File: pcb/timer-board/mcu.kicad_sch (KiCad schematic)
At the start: 7 parts, among them U1 STM32F411RET6

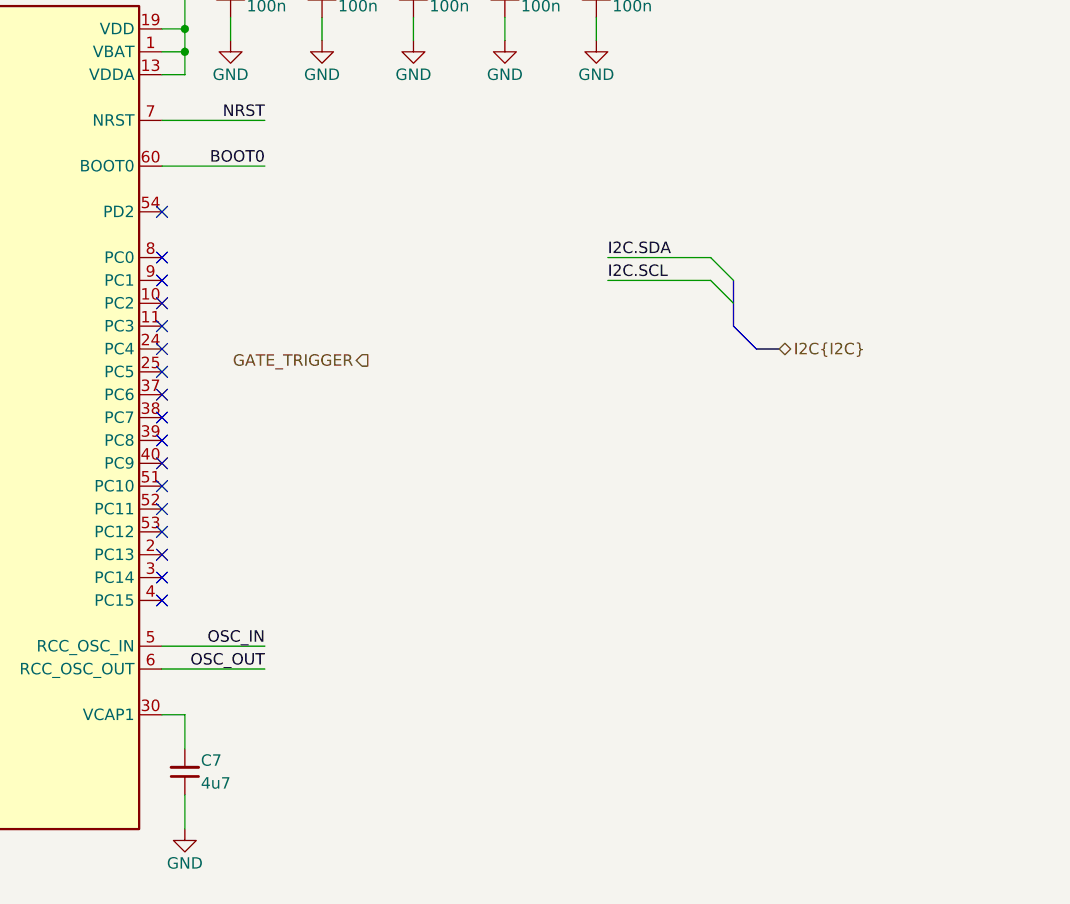
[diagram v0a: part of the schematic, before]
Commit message: Connect OLED display, position main components
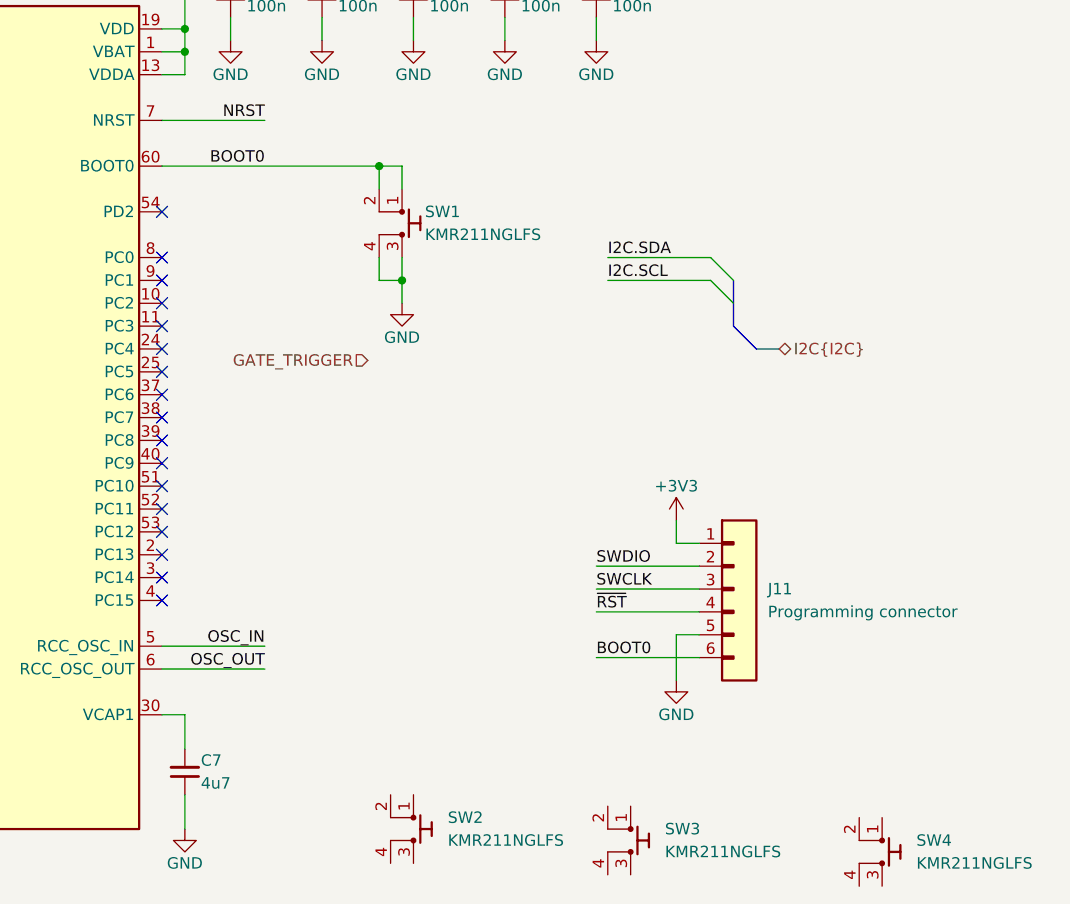
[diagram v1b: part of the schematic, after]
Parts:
- added J11: Programming connector, DW-footprints:Custom-programming-connector-1x6_P1.27mm, symbol DW-connectors:Custom-programming-connector-1x6_P1.27mm
- added SW1, SW2, SW3, SW4: SW_KMR211NGLFS, DW-footprints:SW_KMR211NGLFS, symbol DW-mechanical:SW_KMR211NGLFS
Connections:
- net +3V3: now also J11.1
- net BOOT0: now also J11.6, SW1.1, SW1.2
- net GND: now also J11.5, SW1.3, SW1.4
- net SWCLK: now also J11.3
- net SWDIO: now also J11.2
- new net ~{RST}: J11.4

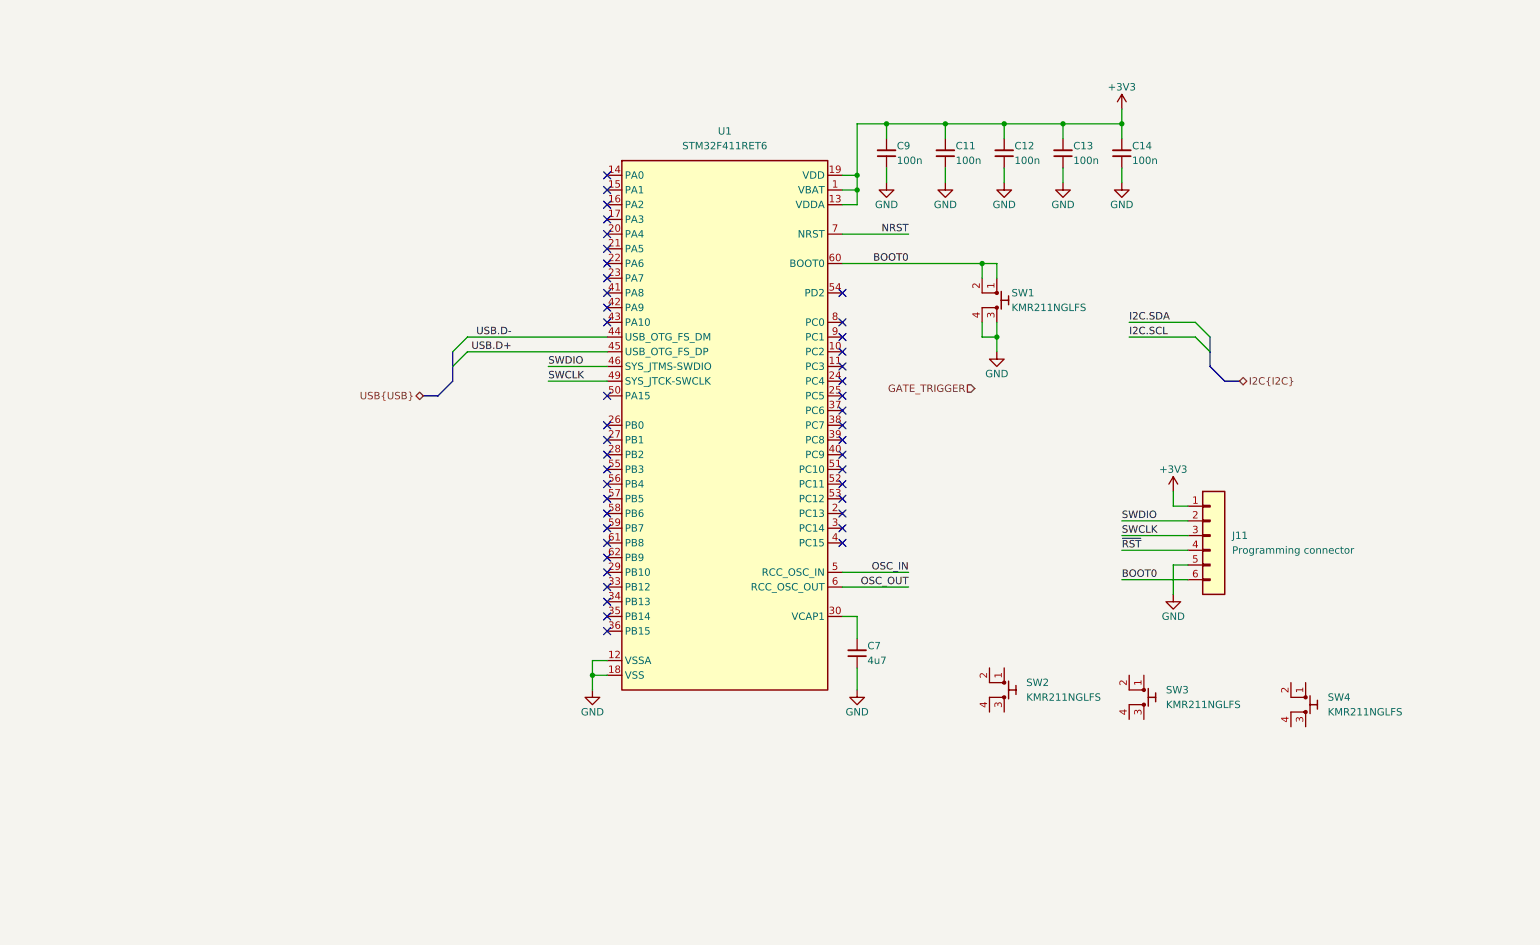
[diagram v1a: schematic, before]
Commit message: Layout power planes and different signals
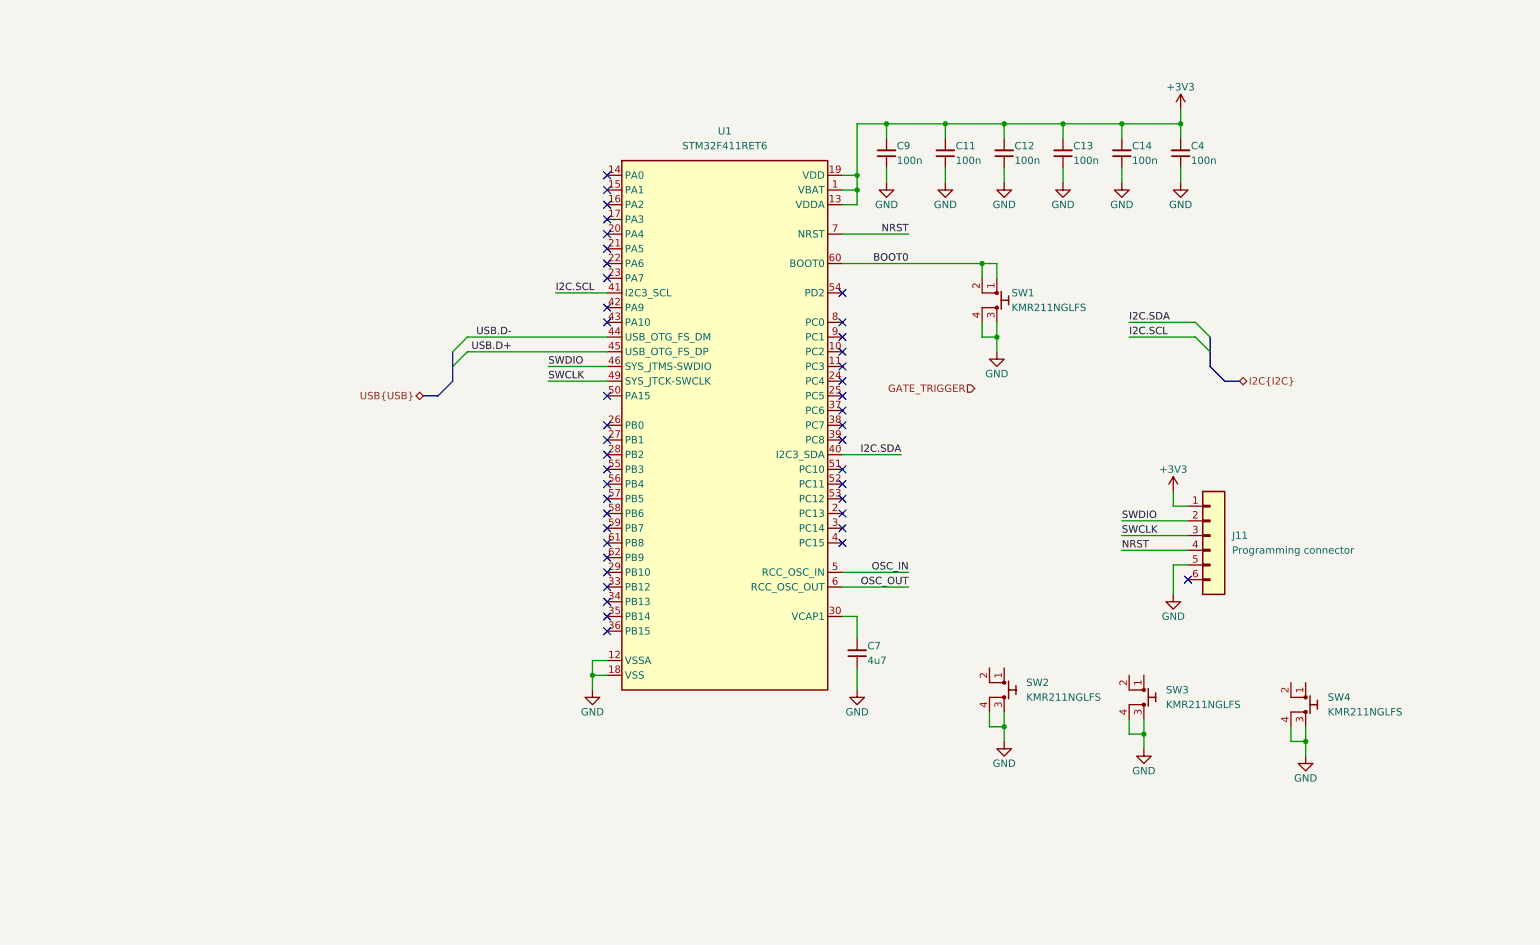
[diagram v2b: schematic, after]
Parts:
- added C4: C-100n-0402, DW-footprints:C_0402_1005Metric, symbol DW-capacitors:C-100n-0402
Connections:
- net ~{RST} is gone; now on net NRST: J11.4
- net +3V3: now also C4.2
- net BOOT0: no longer J11.6
- net GND: now also SW2.3, SW2.4, SW3.3, SW3.4, SW4.3, SW4.4, C4.1
- net I2C.SCL: now also U1.41 (PA8)
- net I2C.SDA: now also U1.40 (PC9)
- no-connect marks 44 -> 43

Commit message: Finish uncompleted schematic sections, layout most of the PCB
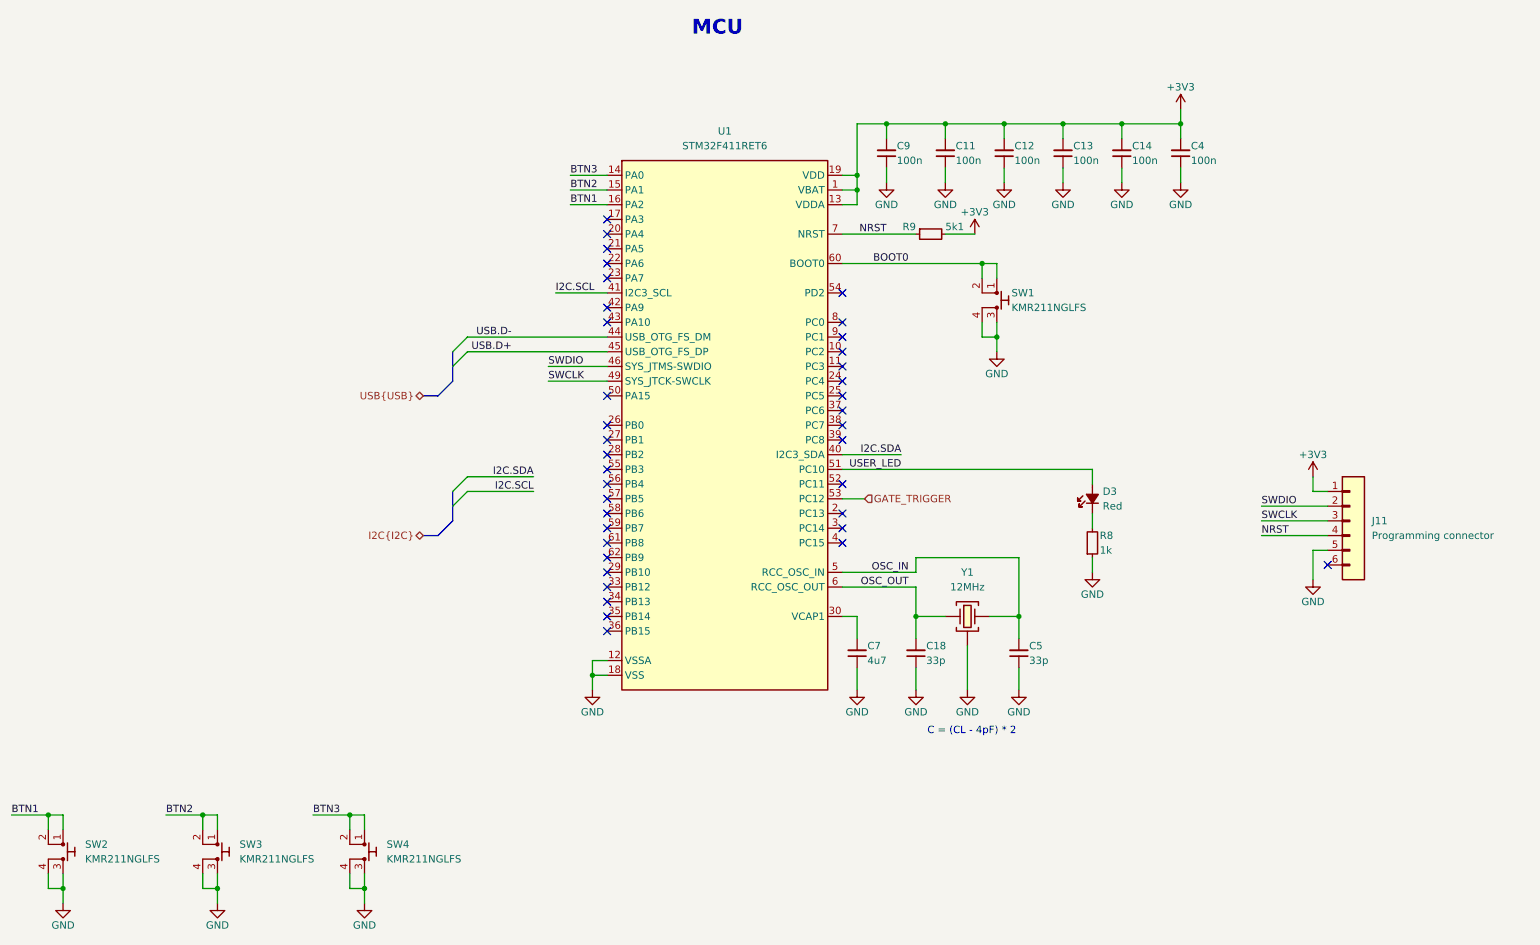
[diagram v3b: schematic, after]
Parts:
- added C18, C5: C-33p-0402, DW-footprints:C_0402_1005Metric, symbol DW-capacitors:C-33p-0402
- added D3: LED-R-0603_KT-0603R, DW-footprints:LED_0603_1608Metric_R, symbol DW-diodes:LED-R-0603_KT-0603R
- added R8: R-1k-0402, DW-footprints:R_0402_1005Metric, symbol DW-resistors:R-1k-0402
- added R9: R-5k1-0402, DW-footprints:R_0402_1005Metric, symbol DW-resistors:R-5k1-0402
- added Y1: X322512MSB4SI, DW-footprints:Crystal_SMD_3225-4Pin_3.2x2.5mm, symbol DW-crystals:Crystal_12MHz_X322512MSB4SI
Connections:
- net +3V3: now also R9.2
- net GATE_TRIGGER: now also U1.53 (PC12)
- net GND: now also C18.1, C5.1, R8.1, Y1.2 (SH), Y1.4 (SH)
- net NRST: now also R9.1
- net OSC_IN: now also C5.2, Y1.3
- net OSC_OUT: now also C18.2, Y1.1
- net BTN3: now reaches SW4.1
- net BTN3: now also SW4.2, U1.14 (PA0)
- net BTN2: now reaches SW3.1
- net BTN2: now also SW3.2, U1.15 (PA1)
- net BTN1: now reaches U1.16 (PA2)
- net BTN1: now also SW2.1, SW2.2
- net USER_LED: now reaches U1.51 (PC10)
- net USER_LED: now also D3.2 (A)
- new net: D3.1 (C), R8.2
- no-connect marks 43 -> 38
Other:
- note added: "C = (CL - 4pF) * 2"
- note added: "MCU"
- moved on the sheet: J11, SW2, SW3, SW4

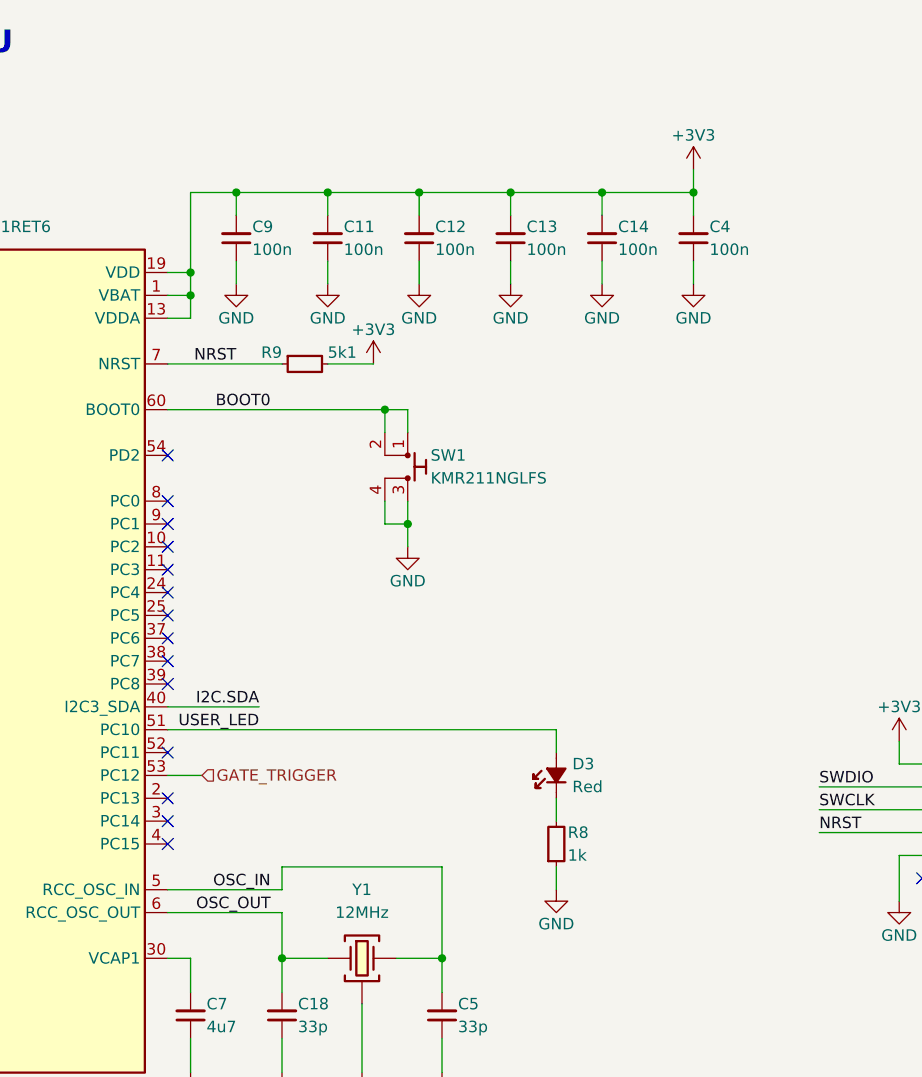
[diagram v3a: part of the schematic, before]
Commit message: Add 3.5mm jack, fix BOOT0 connection
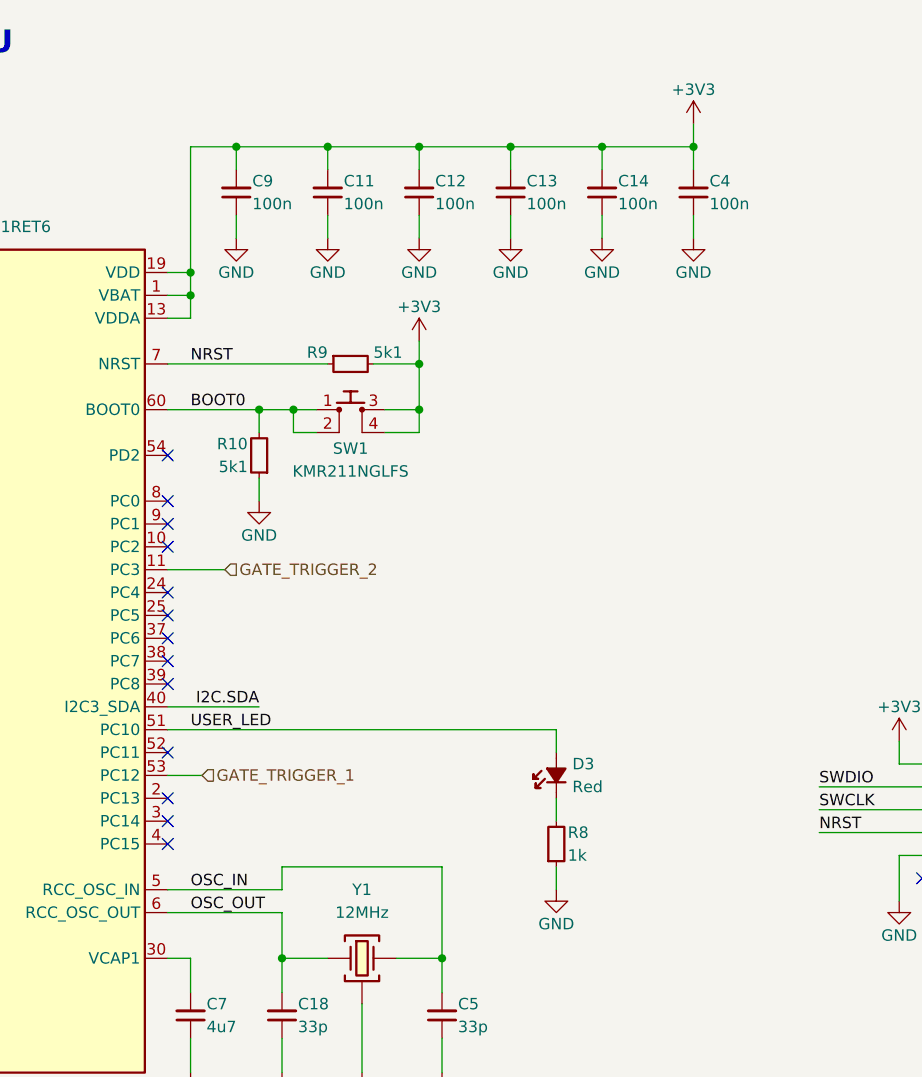
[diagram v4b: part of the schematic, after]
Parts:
- added R10: R-5k1-0402, DW-footprints:R_0402_1005Metric, symbol DW-resistors:R-5k1-0402
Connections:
- net +3V3: now also SW1.3, SW1.4
- net BOOT0: now also R10.2
- net GND: now also R10.1; no longer SW1.3, SW1.4
- net GATE_TRIGGER_2: now reaches U1.11 (PC3)
- net GATE_TRIGGER renamed GATE_TRIGGER_1
- no-connect marks 38 -> 37
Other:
- moved on the sheet: C11, C12, C13, C14, C4, C9, R9, SW1
